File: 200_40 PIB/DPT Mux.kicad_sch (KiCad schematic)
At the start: 18 parts, among them J10 53261-0671, J9 53261-0671, U13 74LVC1G18DBV, U16 74LVC2G157DCU, U17 74LVC1G18DBV

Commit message: prelim layout for pib mainboard v1. TODO review
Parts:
- C52, C53, C54: footprint Capacitor_SMD:C_0603_1608Metric -> Capacitor_SMD:C_0402_1005Metric
- J10, J9: value 53261-0671 -> 53398-0671; footprint Connector_Molex:Molex_PicoBlade_53261-0671_1x06-1MP_P1.25mm_Horizontal -> Connector_Molex:Molex_PicoBlade_53398-0671_1x06-1MP_P1.25mm_Vertical
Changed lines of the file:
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@@
+	)
+	(symbol
+		(lib_id "Connector:Conn_01x06_Pin")
+		(at 208.28 76.2 0)
+		(mirror y)
+		(unit 1)
+		(body_style 1)
+		(exclude_from_sim no)
+		(in_bom yes)
+		(on_board yes)
+		(in_pos_files yes)
+		(dnp no)
+		(fields_autoplaced yes)
+		(property "Reference" "J10"
+			(at 209.55 76.1999 0)
+			(show_name no)
+			(do_not_autoplace no)
+			(effects
+				(font
+					(size 1.27 1.27)
+				)
+				(justify right)
+			)
+		)
+		(property "Value" "53398-0671"
+			(at 209.55 78.7399 0)
+			(show_name no)
+			(do_not_autoplace no)
+			(effects
+				(font
+					(size 1.27 1.27)
+				)
+				(justify right)
+			)
+		)
+		(property "Footprint" "Connector_Molex:Molex_PicoBlade_53398-0671_1x06-1MP_P1.25mm_Vertical"
+			(at 208.28 76.2 0)
+			(hide yes)
+			(show_name no)
+			(do_not_autoplace no)
+			(effects
+				(font
+					(size 1.27 1.27)
+				)
+			)
+		)
+		(property "Datasheet" ""
+			(at 208.28 76.2 0)
+			(hide yes)
+			(show_name no)
+			(do_not_autoplace no)
+			(effects
+				(font
+					(size 1.27 1.27)
+				)
+			)
+		)
+		(property "Description" "Generic connector, single row, 01x06, script generated"
+			(at 208.28 76.2 0)
+			(hide yes)
+			(show_name no)
+			(do_not_autoplace no)
+			(effects
+				(font
+					(size 1.27 1.27)
+				)
+			)
+		)
+		(pin "2"
+		)
+		(pin "6"
+		)
+		(pin "4"
+		)
+		(pin "5"
+		)
+		(pin "3"
+		)
+		(pin "1"
+		)
+		(instances
+			(project "PIB"
+				(path "/2bb2e4a1-de70-477a-a246-143db0a21e08/cc1f88ed-408c-4ec5-ab26-d4cb3df82b9c"
+					(reference "J10")
+					(unit 1)
+				)
+			)
+		)
 	)
 	(symbol
@@
 	)
 	(symbol
-		(lib_id "Connector:Conn_01x06_Pin")
-		(at 208.28 76.2 0)
-		(mirror y)
-		(unit 1)
-		(body_style 1)
-		(exclude_from_sim no)
-		(in_bom yes)
-		(on_board yes)
-		(in_pos_files yes)
-		(dnp no)
-		(fields_autoplaced yes)
-		(property "Reference" "J10"
-			(at 209.55 76.1999 0)
-			(show_name no)
-			(do_not_autoplace no)
-			(effects
-				(font
-					(size 1.27 1.27)
-				)
-				(justify right)
-			)
-		)
-		(property "Value" "53261-0671"
-			(at 209.55 78.7399 0)
-			(show_name no)
-			(do_not_autoplace no)
-			(effects
-				(font
-					(size 1.27 1.27)
-				)
-				(justify right)
-			)
-		)
-		(property "Footprint" "Connector_Molex:Molex_PicoBlade_53261-0671_1x06-1MP_P1.25mm_Horizontal"
-			(at 208.28 76.2 0)
-			(hide yes)
-			(show_name no)
-			(do_not_autoplace no)
-			(effects
-				(font
-					(size 1.27 1.27)
-				)
-			)
-		)
-		(property "Datasheet" ""
-			(at 208.28 76.2 0)
-			(hide yes)
-			(show_name no)
-			(do_not_autoplace no)
-			(effects
-				(font
-					(size 1.27 1.27)
-				)
-			)
-		)
-		(property "Description" "Generic connector, single row, 01x06, script generated"
-			(at 208.28 76.2 0)
-			(hide yes)
-			(show_name no)
-			(do_not_autoplace no)
-			(effects
-				(font
-					(size 1.27 1.27)
-				)
-			)
-		)
-		(pin "2"
-		)
-		(pin "6"
-		)
-		(pin "4"
-		)
-		(pin "5"
-		)
-		(pin "3"
-		)
-		(pin "1"
-		)
-		(instances
-			(project "PIB"
-				(path "/2bb2e4a1-de70-477a-a246-143db0a21e08/cc1f88ed-408c-4ec5-ab26-d4cb3df82b9c"
-					(reference "J10")
-					(unit 1)
-				)
-			)
-		)
-	)
-	(symbol
 		(lib_id "power:GND")
 		(at 177.8 73.66 0)
@@
 			)
 		)
-		(property "Footprint" "Capacitor_SMD:C_0603_1608Metric"
+		(property "Footprint" "Capacitor_SMD:C_0402_1005Metric"
 			(at 127.9652 69.85 0)
 			(hide yes)
@@
 			)
 		)
-		(property "Footprint" "Capacitor_SMD:C_0603_1608Metric"
+		(property "Footprint" "Capacitor_SMD:C_0402_1005Metric"
 			(at 106.3752 113.03 0)
 			(hide yes)
@@
 			)
 		)
-		(property "Value" "53261-0671"
+		(property "Value" "53398-0671"
 			(at 209.55 58.4199 0)
 			(show_name no)
@@
 			)
 		)
-		(property "Footprint" "Connector_Molex:Molex_PicoBlade_53261-0671_1x06-1MP_P1.25mm_Horizontal"
+		(property "Footprint" "Connector_Molex:Molex_PicoBlade_53398-0671_1x06-1MP_P1.25mm_Vertical"
 			(at 208.28 55.88 0)
 			(hide yes)
@@
 			)
 		)
-		(property "Footprint" "Capacitor_SMD:C_0603_1608Metric"
+		(property "Footprint" "Capacitor_SMD:C_0402_1005Metric"
 			(at 120.3452 100.33 0)
 			(hide yes)

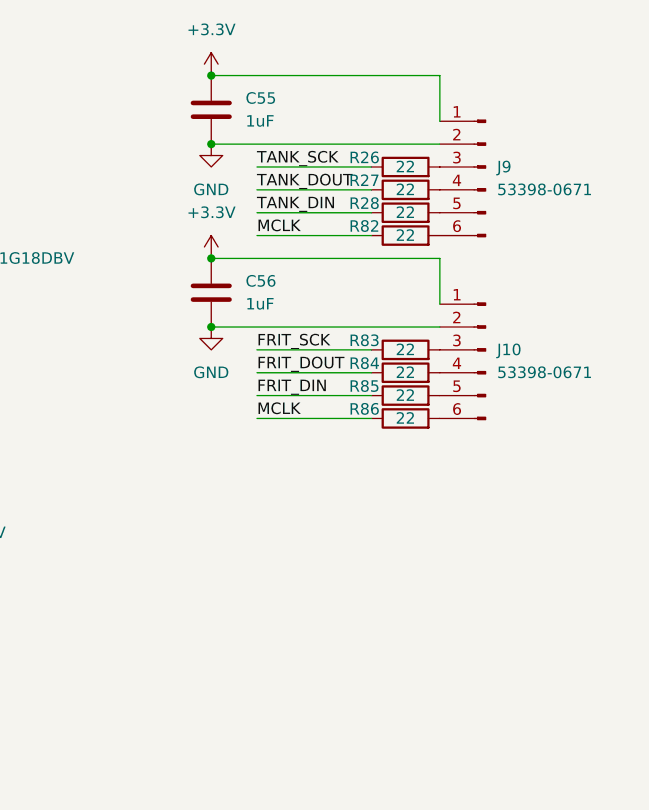
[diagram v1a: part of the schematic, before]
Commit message: fix DRC warnings, check DRC rules against JLC spec, replace all connector symbols with proper MP symbols (MP to ground), fix ground stitching
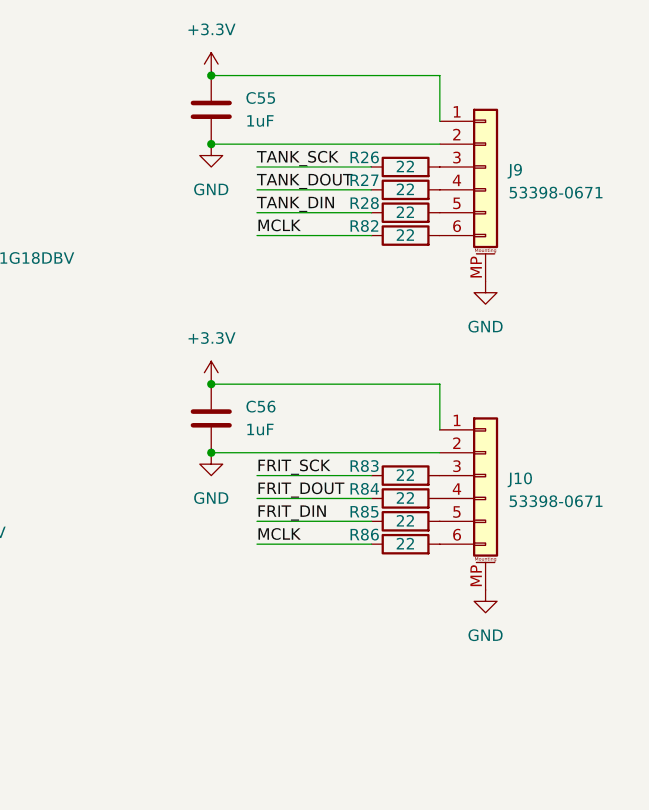
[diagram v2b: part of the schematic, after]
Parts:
- removed J10, J9: 53398-0671, Connector_Molex:Molex_PicoBlade_53398-0671_1x06-1MP_P1.25mm_Vertical, symbol Connector:Conn_01x06_Pin
- added J10, J9: 53398-0671, Connector_Molex:Molex_PicoBlade_53398-0671_1x06-1MP_P1.25mm_Vertical, symbol Connector_Generic_MountingPin:Conn_01x06_MountingPin
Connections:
- net +3.3V: now also J10.1 (Pin_1), J9.1 (Pin_1)
- net GND: now also J10.2 (Pin_2), J10.MP (MountPin), J9.2 (Pin_2), J9.MP (MountPin)
- net at R28.2: now also J9.5 (Pin_5)
- net at R83.2: now also J10.3 (Pin_3)
- net at R84.2: now also J10.4 (Pin_4)
- net at R85.2: now also J10.5 (Pin_5)
- net at R86.2: now also J10.6 (Pin_6)
- net at R26.2: now also J9.3 (Pin_3)
- net at R27.2: now also J9.4 (Pin_4)
- net at R82.2: now also J9.6 (Pin_6)
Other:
- moved on the sheet: C56, R83, R84, R85, R86

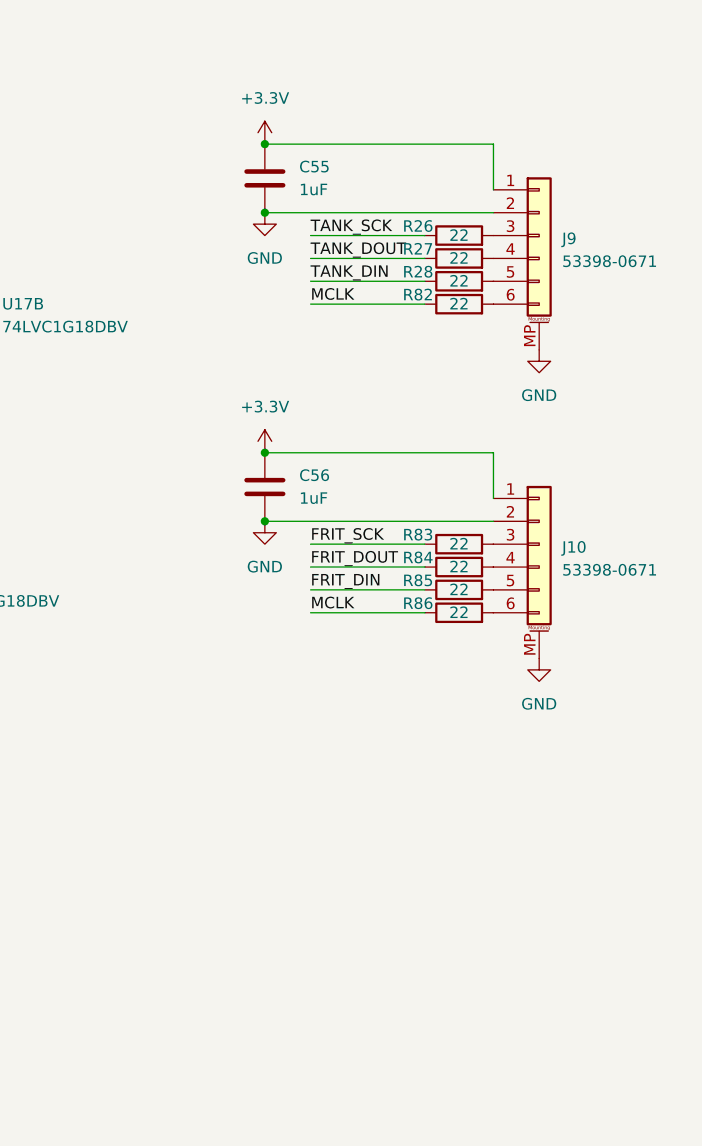
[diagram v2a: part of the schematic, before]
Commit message: add TVS diodes
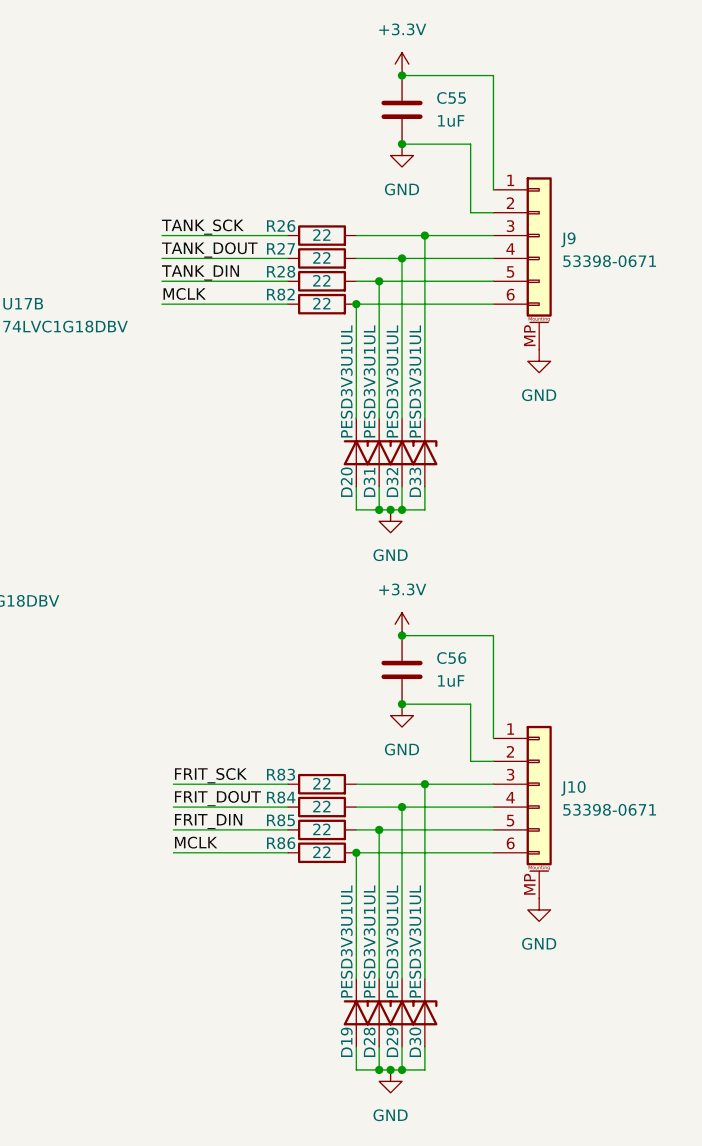
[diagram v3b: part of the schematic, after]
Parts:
- added D19, D20, D28, D29, D30, D31, D32, D33: PESD3V3U1UL, Diode_SMD:D_SOD-882, symbol Diode:PESD3V3U1UL
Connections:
- net GND: now also D19.2 (A), D20.2 (A), D28.2 (A), D29.2 (A), D30.2 (A), D31.2 (A), D32.2 (A), D33.2 (A)
- net at J9.5 (Pin_5), R28.2: now also D31.1 (K)
- net at J10.3 (Pin_3), R83.2: now also D30.1 (K)
- net at J10.4 (Pin_4), R84.2: now also D29.1 (K)
- net at J10.5 (Pin_5), R85.2: now also D28.1 (K)
- net at J10.6 (Pin_6), R86.2: now also D19.1 (K)
- net at J9.3 (Pin_3), R26.2: now also D33.1 (K)
- net at J9.4 (Pin_4), R27.2: now also D32.1 (K)
- net at J9.6 (Pin_6), R82.2: now also D20.1 (K)
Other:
- moved on the sheet: C55, C56, J10

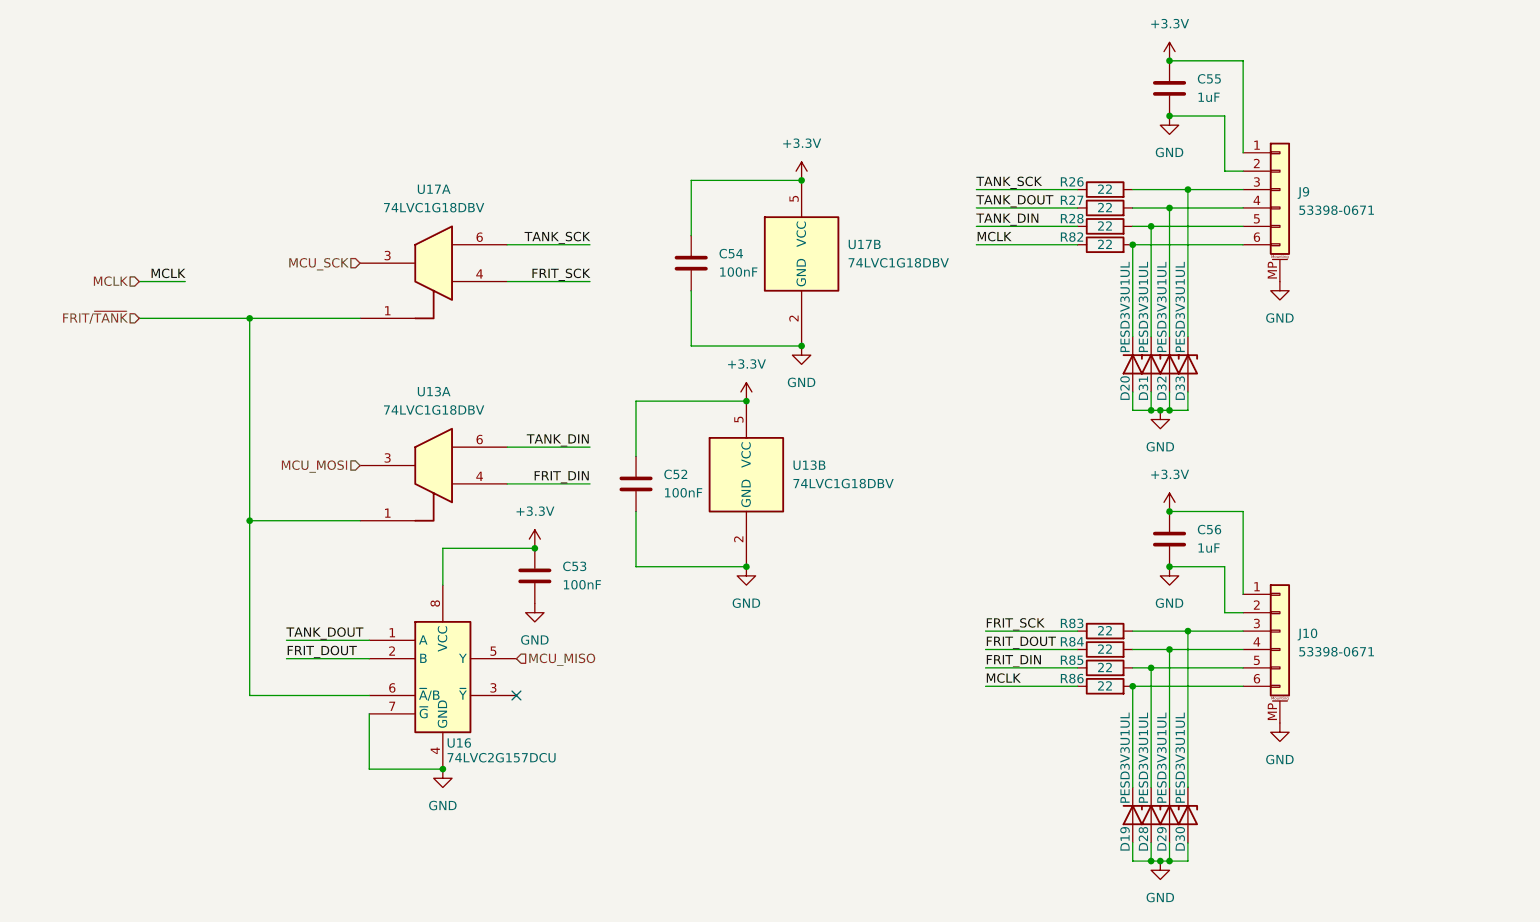
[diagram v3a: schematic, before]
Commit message: fix GSE valve having no power path, fix arm/safe gate floating on reset, fix resistor OR on GSE NC valve, add NC valve flyback diode, change DPT MCLK source to a timer off of HSE, fix crystal load capacitances
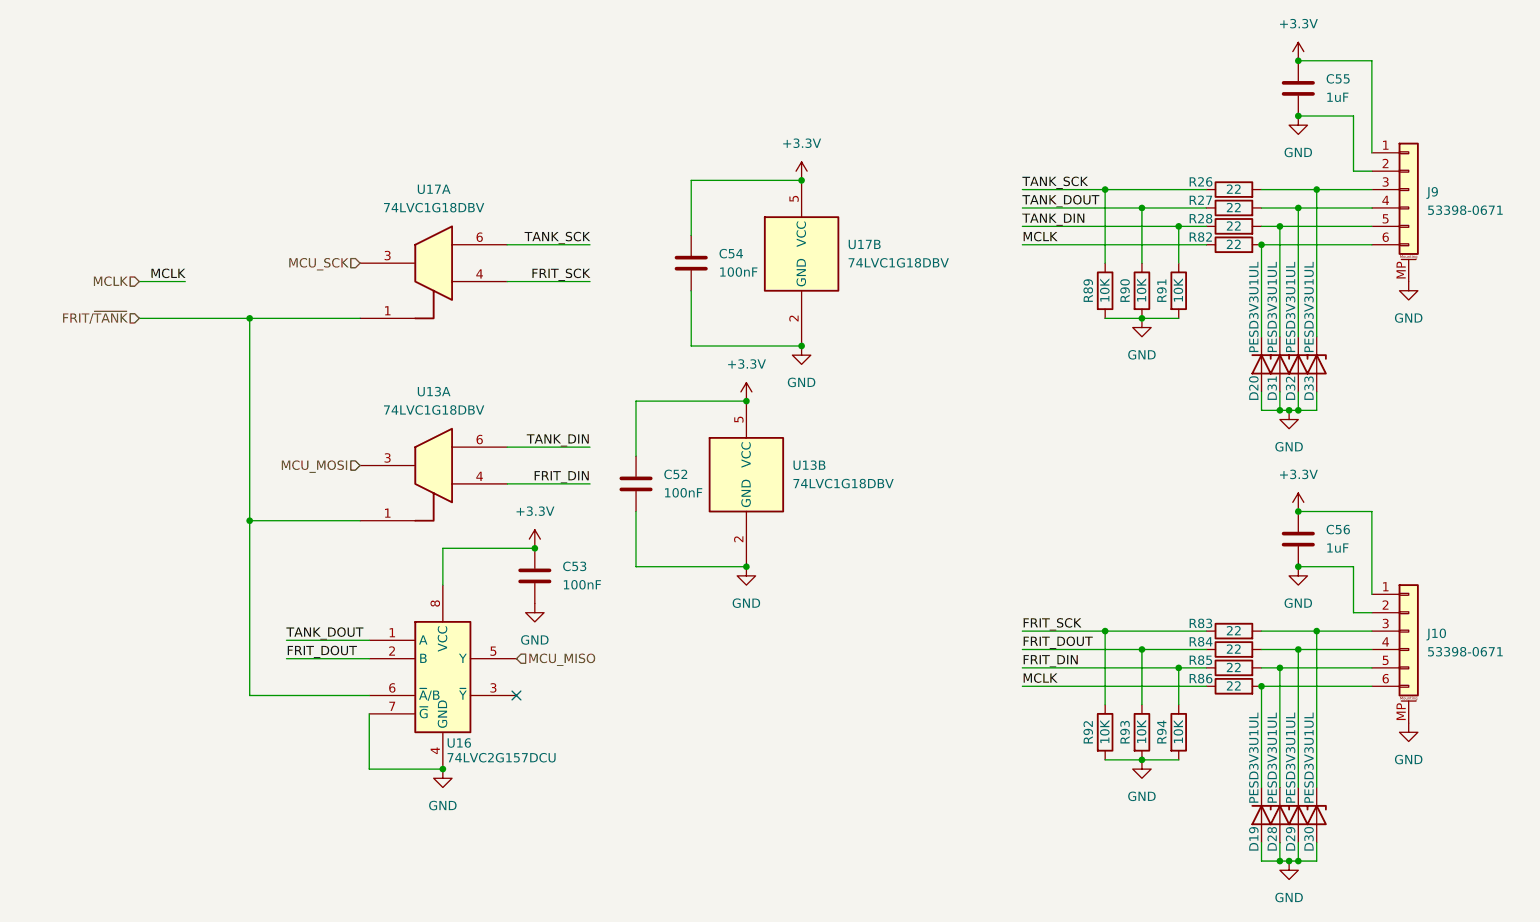
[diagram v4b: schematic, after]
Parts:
- added R89, R90, R91, R92, R93, R94: 10K, Resistor_SMD:R_0402_1005Metric, symbol Device:R
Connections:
- net FRIT_DIN: now also R94.1
- net FRIT_DOUT: now also R93.1
- net FRIT_SCK: now also R92.1
- net GND: now also R89.2, R90.2, R91.2, R92.2, R93.2, R94.2
- net TANK_DIN: now also R91.1
- net TANK_DOUT: now also R90.1
- net TANK_SCK: now also R89.1
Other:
- moved on the sheet: C55, C56, D19, D20, D28, D29, D30, D31, D32, D33, J10, J9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

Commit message: Assign MPNs and digikey PNs, export gerbers & bom. PIB Mainboard Rev 1.0 Release
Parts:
- C52, C53, C54: Digikey PN (none) -> 490-10672-1-ND; MP (none) -> GCM155R71H104KE02D
- C55, C56: Digikey PN (none) -> 587-3352-1-ND; MP (none) -> GMK107AB7105KAHT
- D19, D20, D28, D29, D30, D31, D32, D33: Digikey PN (none) -> 1727-4154-1-ND; MP (none) -> PESD3V3U1UL,315
- J10, J9: Digikey PN (none) -> WM7610CT-ND; MP (none) -> 53398-0671
- R26, R27, R28, R82, R83, R84, R85, R86: Digikey PN (none) -> 311-22.0LRCT-ND; MP (none) -> RC0402FR-0722RL
- R89, R90, R91, R92, R93, R94: Digikey PN (none) -> YAG1346CT-ND; MP (none) -> RT0402BRD0710KL
- U13, U17: Digikey PN (none) -> 296-15568-1-ND; MP (none) -> SN74LVC1G18DBVR
- U16: Digikey PN (none) -> 296-12605-1-ND; MP (none) -> SN74LVC2G157DCUR
